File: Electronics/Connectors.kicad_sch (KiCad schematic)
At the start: 0 parts

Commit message: Added third half bridge for BLDC applications
Signed-off-by: Finder <aki.kuusela@findersee.fi>
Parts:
- added C501, C502, C503: 100n, Capacitor_SMD:C_0603_1608Metric_Pad1.08x0.95mm_HandSolder, symbol Device:C_Small
- added F501: 20A, Fuse:Fuse_Blade_Mini_directSolder, symbol Device:Fuse
- added J501, J502: Conn_01x06_Female, TerminalBlock:TerminalBlock_bornier-6_P5.08mm, symbol Connector:Conn_01x06_Female
- added R501, R502, R503: 100, Resistor_SMD:R_0603_1608Metric_Pad0.98x0.95mm_HandSolder, symbol Device:R
- added R504, R505, R506: 11k, Resistor_SMD:R_0603_1608Metric_Pad0.98x0.95mm_HandSolder, symbol Device:R
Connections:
- new net: F501.2, J502.1 (Pin_1)
- new net: C501.1, J501.1 (Pin_1), R501.1
- new net: C502.1, J501.3 (Pin_3), R502.1
- new net: C503.1, J501.5 (Pin_5), R503.1
- new net +3V3: R504.1, R505.1, R506.1
- new net Button: R503.2, R506.2
- new net GND: C501.2, C502.2, C503.2, J501.2 (Pin_2), J501.4 (Pin_4), J501.6 (Pin_6), J502.2 (Pin_2)
- new net Limit 1: R501.2, R504.2
- new net Limit 2: R502.2, R505.2
- new net MOTOR C: J502.4 (Pin_4)
- new net MOTOR NEG: J502.5 (Pin_5)
- new net MOTOR POS: J502.6 (Pin_6)
- new net Vdrive: F501.1
- no-connect marks 0 -> 1

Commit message: Layout update
Signed-off-by: Aki Kuusela <git@findersee.fi>
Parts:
- J502: value Conn_01x06_Female -> Motor Con
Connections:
- net GND: now also J502.5 (Pin_5); no longer J502.2 (Pin_2)
- net MOTOR C: now also J502.3 (Pin_3); no longer J502.4 (Pin_4)
- net MOTOR NEG: now also J502.2 (Pin_2); no longer J502.5 (Pin_5)
- net MOTOR POS: now also J502.1 (Pin_1); no longer J502.6 (Pin_6)
- net at F501.2: now also J502.6 (Pin_6); no longer J502.1 (Pin_1)
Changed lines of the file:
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@@
     (pin "2")
   )
-  (symbol (lib_id "Connector:Conn_01x06_Female") (at 229.87 73.66 0) (unit 1)
+  (symbol (lib_id "Connector:Conn_01x06_Female") (at 229.87 76.2 0) (mirror x) (unit 1)
     (in_bom yes) (on_board yes) (fields_autoplaced)
-    (property "Reference" "J502" (id 0) (at 230.5812 74.0215 0)
-      (effects (font (size 1.27 1.27)) (justify left))
-    )
-    (property "Value" "Conn_01x06_Female" (id 1) (at 230.5812 76.7966 0)
-      (effects (font (size 1.27 1.27)) (justify left))
-    )
-    (property "Footprint" "TerminalBlock:TerminalBlock_bornier-6_P5.08mm" (id 2) (at 229.87 73.66 0)
+    (property "Reference" "J502" (id 0) (at 229.235 63.5 0))
+    (property "Value" "Motor Con" (id 1) (at 229.235 66.04 0))
+    (property "Footprint" "TerminalBlock:TerminalBlock_bornier-6_P5.08mm" (id 2) (at 229.87 76.2 0)
       (effects (font (size 1.27 1.27)) hide)
     )
-    (property "Datasheet" "~" (id 3) (at 229.87 73.66 0)
+    (property "Datasheet" "~" (id 3) (at 229.87 76.2 0)
       (effects (font (size 1.27 1.27)) hide)
     )

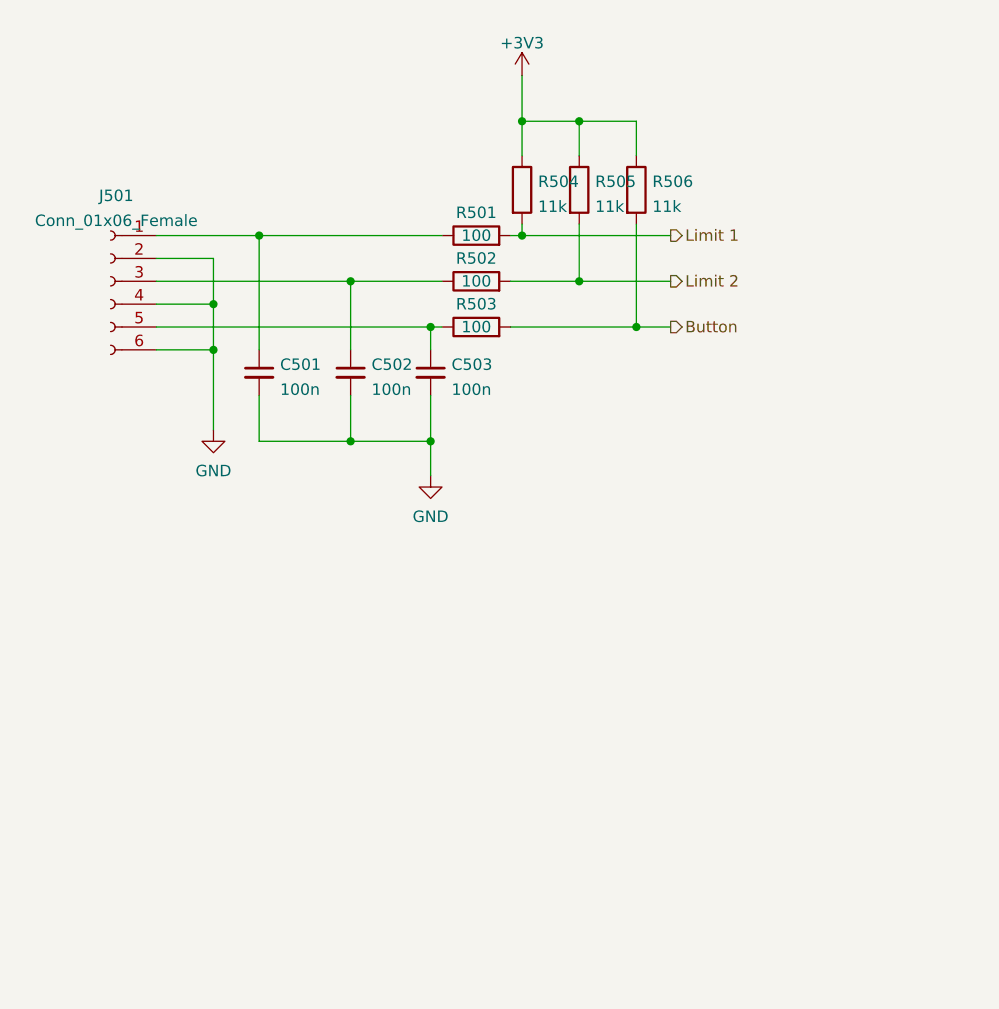
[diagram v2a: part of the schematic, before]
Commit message: Added hall sensor circuitry
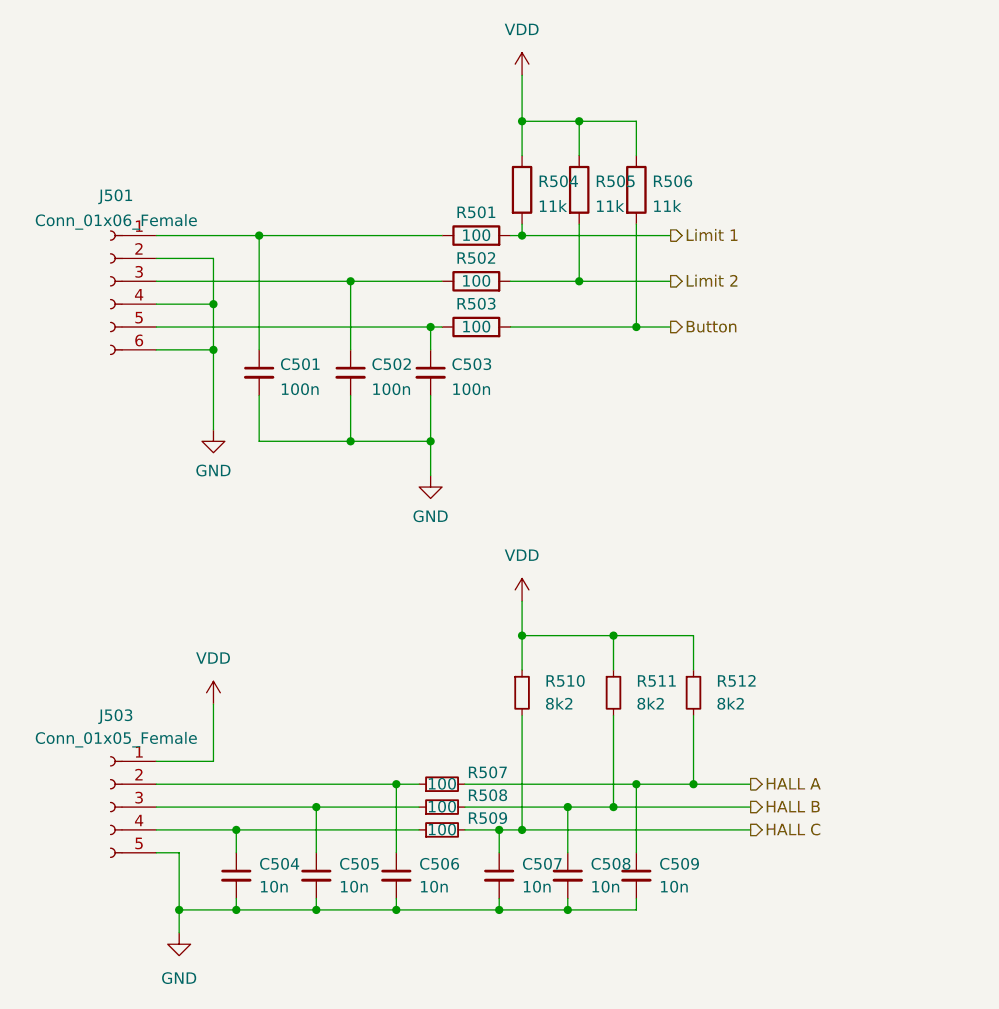
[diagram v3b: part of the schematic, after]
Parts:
- added C504, C505, C506, C507, C508, C509: 10n, Capacitor_SMD:C_0603_1608Metric_Pad1.08x0.95mm_HandSolder, symbol Device:C_Small
- added J503: Conn_01x05_Female, Connector_PinHeader_2.54mm:PinHeader_1x05_P2.54mm_Vertical, symbol Connector:Conn_01x05_Female
- added R507, R508, R509: 100, Resistor_SMD:R_0603_1608Metric_Pad0.98x0.95mm_HandSolder, symbol Device:R_Small
- added R510, R511, R512: 8k2, Resistor_SMD:R_0603_1608Metric_Pad0.98x0.95mm_HandSolder, symbol Device:R_Small
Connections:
- net GND: now also C504.2, C505.2, C506.2, C507.2, C508.2, C509.2, J503.5 (Pin_5)
- net +3V3 renamed VDD
- net VDD: now also J503.1 (Pin_1), R510.1, R511.1, R512.1
- new net: C504.1, J503.4 (Pin_4), R509.1
- new net: C505.1, J503.3 (Pin_3), R508.1
- new net: C506.1, J503.2 (Pin_2), R507.1
- new net HALL A: C509.1, R507.2, R512.2
- new net HALL B: C508.1, R508.2, R511.2
- new net HALL C: C507.1, R509.2, R510.2

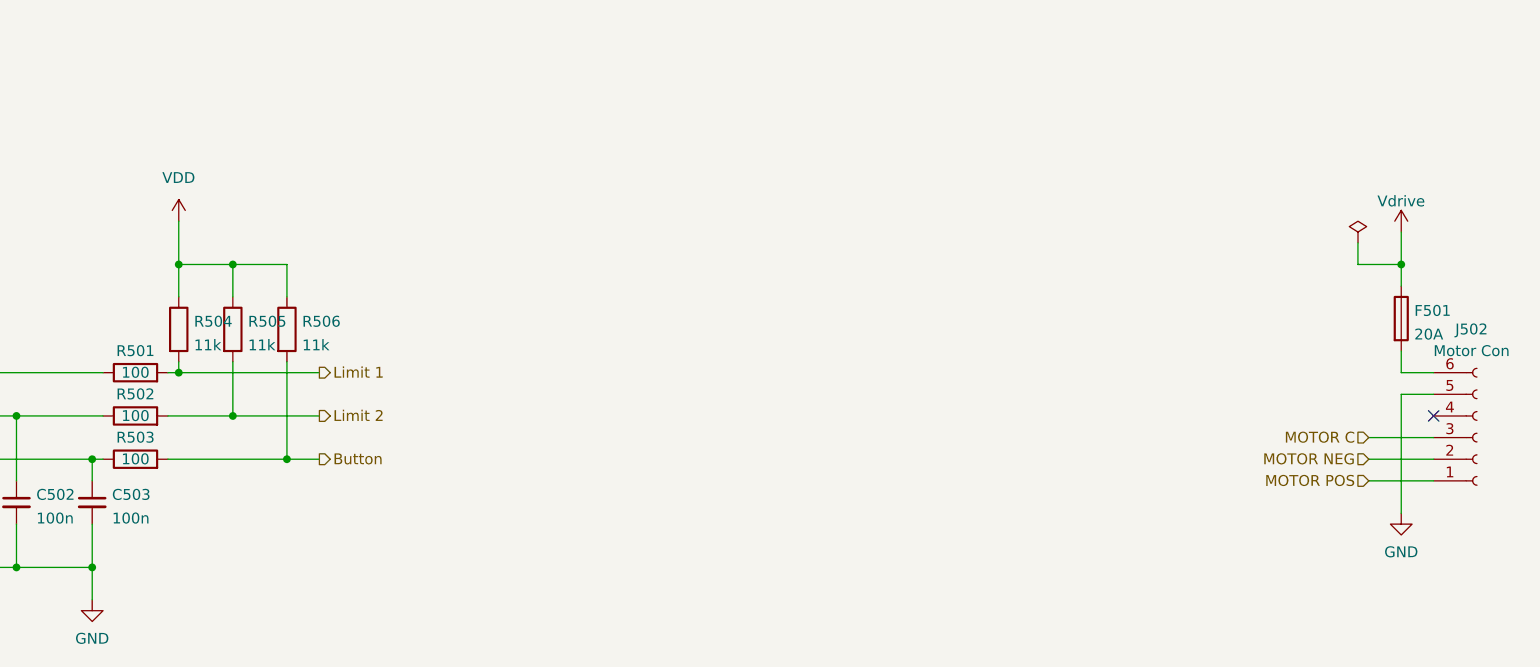
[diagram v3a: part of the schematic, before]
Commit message: Added Current sensor finalized layout version 0.1
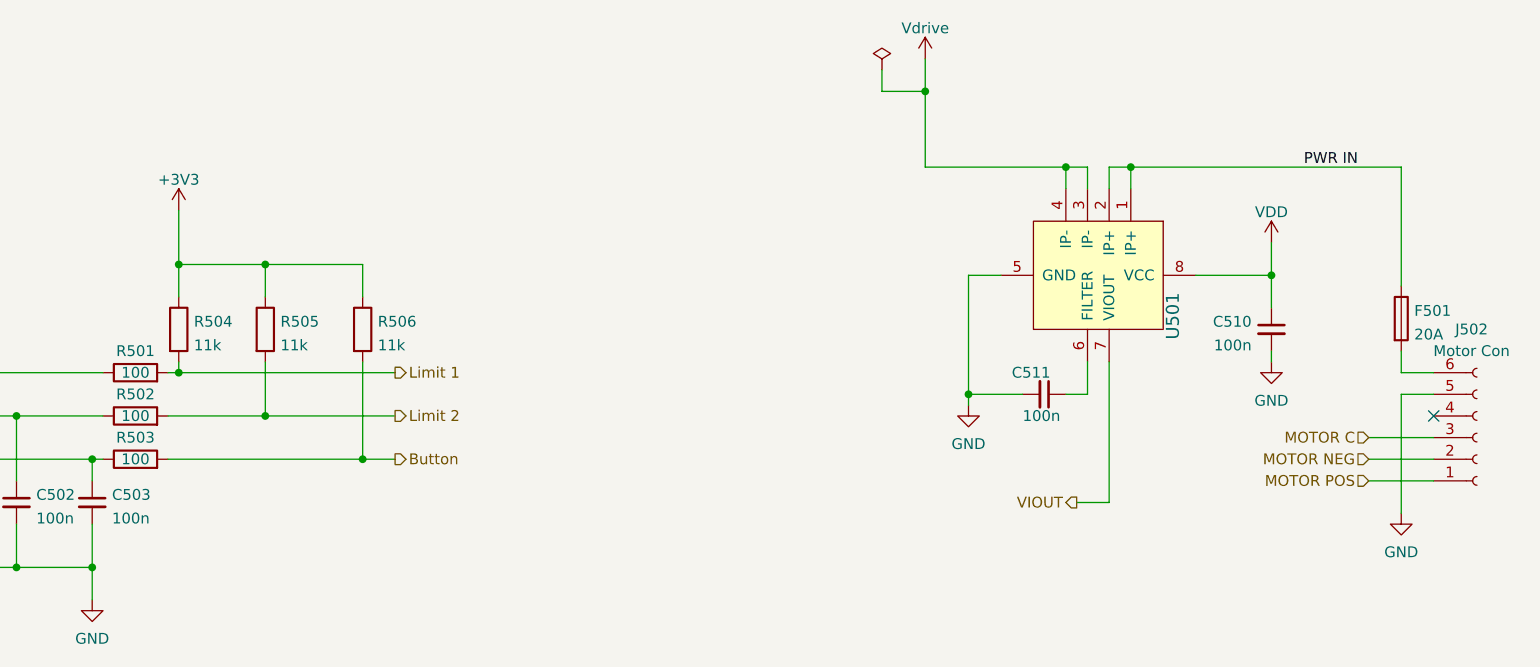
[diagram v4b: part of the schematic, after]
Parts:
- added C510, C511: 100n, Capacitor_SMD:C_0603_1608Metric_Pad1.08x0.95mm_HandSolder, symbol Device:C_Small
- added U501: ACS712ELCTR-20A-T_NRND, digikey-footprints:SOIC-8_W3.9mm, symbol dk_Current-Sensors:ACS712ELCTR-20A-T_NRND
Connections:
- net GND: now also C510.2, C511.2, U501.5 (GND)
- net VDD: now also C510.1, U501.8 (VCC); no longer R504.1, R505.1, R506.1
- net Vdrive: now also U501.3 (IP-), U501.4 (IP-); no longer F501.1
- new net: C511.1, U501.6 (FILTER)
- new net +3V3: R504.1, R505.1, R506.1
- new net PWR IN: F501.1, U501.1 (IP+), U501.2 (IP+)
- new net VIOUT: U501.7 (VIOUT)
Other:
- moved on the sheet: R505, R506

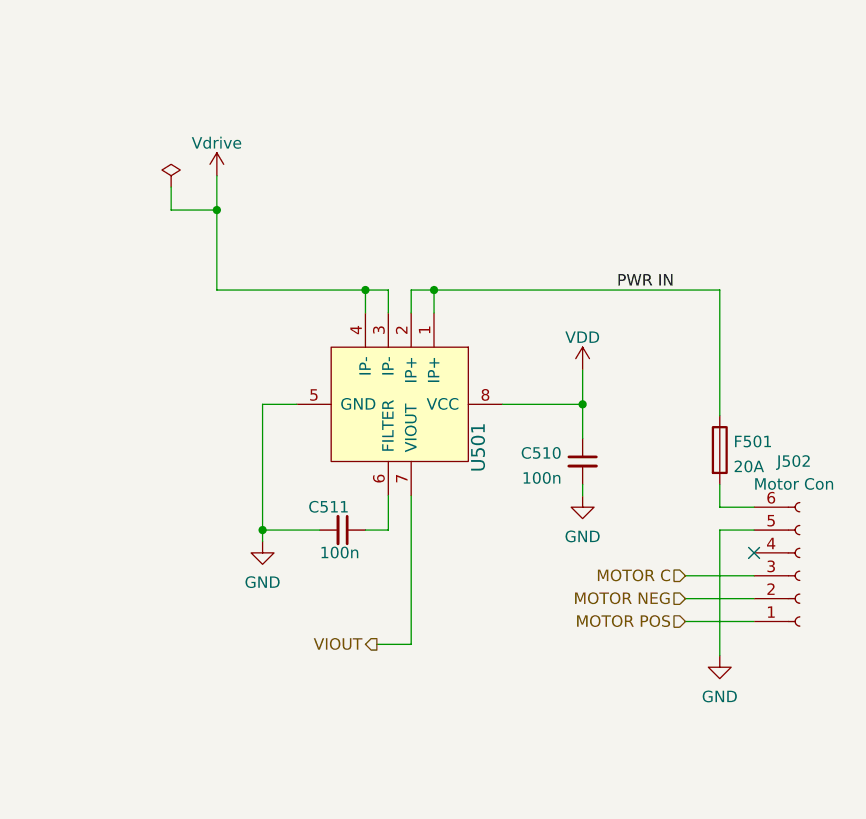
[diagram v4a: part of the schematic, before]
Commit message: Added current sensor circuitry
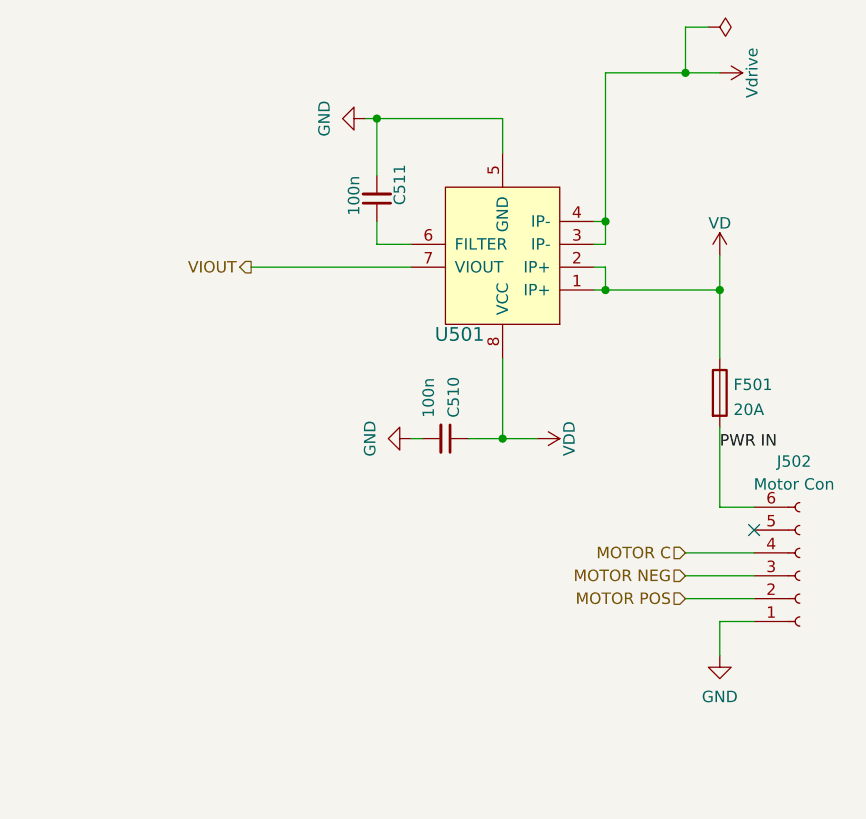
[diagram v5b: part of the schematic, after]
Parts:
- F501: footprint Fuse:Fuse_Blade_Mini_directSolder -> digikey-footprints:3550-2_KEYS
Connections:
- net GND: now also J502.1 (Pin_1); no longer J502.5 (Pin_5)
- net MOTOR C: now also J502.4 (Pin_4); no longer J502.3 (Pin_3)
- net MOTOR NEG: now also J502.3 (Pin_3); no longer J502.2 (Pin_2)
- net MOTOR POS: now also J502.2 (Pin_2); no longer J502.1 (Pin_1)
- net PWR IN: now also F501.2, J502.6 (Pin_6); no longer F501.1, U501.1 (IP+), U501.2 (IP+)
- new net VD: F501.1, U501.1 (IP+), U501.2 (IP+)
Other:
- moved on the sheet: C510, C511, F501, U501

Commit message: Updated Design
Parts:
- removed U501: ACS712ELCTR-20A-T_NRND, digikey-footprints:SOIC-8_W3.9mm, symbol dk_Current-Sensors:ACS712ELCTR-20A-T_NRND
- added C512, C514, C515, C516: 100n, Capacitor_SMD:C_0603_1608Metric_Pad1.08x0.95mm_HandSolder, symbol Device:C
- added C513: 10n, Capacitor_SMD:C_0603_1608Metric_Pad1.08x0.95mm_HandSolder, symbol Device:C_Small
- added D501: 1N5819, Diode_SMD:D_SOD-123, symbol Diode:1N5819
- added D502: LED, LED_SMD:LED_1206_3216Metric_Pad1.42x1.75mm_HandSolder, symbol Device:LED
- added Q501: BC817, Package_TO_SOT_SMD:SOT-23, symbol Transistor_BJT:BC817
- added R513, R514, R517, R519: 11k, Resistor_SMD:R_0603_1608Metric_Pad0.98x0.95mm_HandSolder, symbol Device:R
- added R515: 10k, Resistor_SMD:R_0603_1608Metric_Pad0.98x0.95mm_HandSolder, symbol Device:R
- added R516: 0, Resistor_SMD:R_0603_1608Metric_Pad0.98x0.95mm_HandSolder, symbol Device:R
- added R518: 1k, LED_SMD:LED_0603_1608Metric_Pad1.05x0.95mm_HandSolder, symbol Device:R_Small
- added R520: 100k, Resistor_SMD:R_0603_1608Metric_Pad0.98x0.95mm_HandSolder, symbol Device:R
- added RV501: 50k, Potentiometer_SMD:Potentiometer_Vishay_TS53YJ_Vertical, symbol Device:R_Potentiometer_Trim
- added S501: B3U-1000P, digikey-footprints:Switch_Tactile_SMD_B3U-1000P, symbol dk_Tactile-Switches:B3U-1000P
- added TP501, TP505, TP507: GND, TestPoint:TestPoint_Pad_1.5x1.5mm, symbol Connector:TestPoint_Small
- added TP502: Current Out Att, TestPoint:TestPoint_Pad_D1.0mm, symbol Connector:TestPoint_Small
- added TP503: Current Out, TestPoint:TestPoint_Pad_D1.0mm, symbol Connector:TestPoint_Small
- added TP504: Current Out AMP, TestPoint:TestPoint_Pad_D1.0mm, symbol Connector:TestPoint
- added TP506: Current Limit, TestPoint:TestPoint_Pad_D1.0mm, symbol Connector:TestPoint_Small
- added U501: ‎ACHS-7124-000E‎, Package_SO:SO-8_3.9x4.9mm_P1.27mm, symbol Findersee_parts:‎ACHS-7124-000E‎
- added U502: LM393, Package_SO:SO-8_3.9x4.9mm_P1.27mm, symbol Comparator:LM393
- added U503: 74AHC08, Package_SO:SO-14_3.9x8.65mm_P1.27mm, symbol 74xx:74LS08
- added U504: MCP6001-OT, Package_TO_SOT_SMD:SOT-23-5, symbol Amplifier_Operational:MCP6001-OT
- J501: value Conn_01x06_Female -> Switches
- J503: value Conn_01x05_Female -> Hall Sensor
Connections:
- net +3V3: now also C512.2, U502.5 (+), U503.14 (VCC); no longer R504.1, R505.1
- net GND: now also C511.1, C512.1, C513.2, C514.1, C515.1, C516.1, Q501.2 (E), R514.2, R519.2, RV501.3, S501.1, TP501.1, TP505.1, TP507.1, U501.5 (GND), U502.4 (V-), U502.6 (_), U503.10, U503.12, U503.13, U503.7 (GND), U503.9, U504.2 (V-); no longer C511.2
- net Limit 1: now also U503.6; no longer R501.2, R504.2
- net Limit 2: now also U503.3; no longer R502.2, R505.2
- net VD: now also U501.1 (IP+), U501.2 (IP+)
- net VDD: now also R504.1, R505.1, C514.2, C515.2, R517.1, R518.1, RV501.1, U501.8 (VDD), U502.8 (V+), U504.5 (V+)
- net VIOUT: now also R516.1
- net Vdrive: now also U501.3 (IP-), U501.4 (IP-)
- new net: Q501.1 (B), R520.1
- new net: C511.2, U501.6 (Filter)
- new net: R513.1, TP503.1, U501.7 (Vout)
- new net: D501.1 (K), D502.1 (K), R517.2, U502.1, U503.1, U503.4
- new net: D502.2 (A), R518.2
- new net: R515.2, R516.2, TP504.1, U504.1, U504.4 (-)
- new net: C513.1, R513.2, R514.1, TP502.1, U504.3 (+)
- new net: Q501.3 (C), R515.1, S501.2, U502.2 (-)
- new net: C516.2, D501.2 (A), RV501.2, TP506.1, U502.3 (+)
- new net LIMIT 1: R501.2, R504.2, U503.5
- new net LIMIT 2: R502.2, R505.2, U503.2
- new net Latch Reset: R519.1, R520.2
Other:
- note added: "Manual Reset"
- moved on the sheet: C510, C511, F501, J502
